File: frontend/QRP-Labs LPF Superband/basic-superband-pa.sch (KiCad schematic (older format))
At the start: 67 parts, among them CN1 EDGE, K1 D3002, K2 D3002, P1 BNC, P2 VFWD, P3 Ext PTT, P4 12-13.8v, Q1 FDV301, Q2 FDV301, Q3 RD16HHF1, T2 8:1, T3 4:1, T4 OUT_TRANSF, U1 LP2951-50D

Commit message: New pre-v2 files
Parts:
- removed C2, C3: 0.1 uF, HERMESLITE:C_0805, symbol Csmall
- removed C26, C4: 0.1uF, HERMESLITE:C_0805, symbol C
- removed CN1: EDGE, HERMESLITE:EDGE, symbol EDGE
- removed D1: YEL LED (Band1), LEDs:LED-0805, symbol LED
- removed D2: RED LED (PTT), LEDs:LED-0805, symbol LED
- removed D3: GRN LED (PWR ON), LEDs:LED-0805, symbol LED
- removed D4: DIODESCH2, HERMESLITE:SOD323, symbol DIODESCH2
- removed FB1: FB, Resistors_SMD:R_0805_HandSoldering, symbol FB
- removed K1, K2: D3002, HERMESLITE:D3002, symbol D3002
- removed P? (x4): CONN_01X04, symbol CONN_01X04
- removed Q1, Q2: FDV301, HERMESLITE:SOT-23-GDS, symbol MOSFET_N
- removed R1, R2: 499, Resistors_SMD:R_0805_HandSoldering, symbol R
- removed R13, R14, R3, R9: 4.99k, Resistors_SMD:R_0805_HandSoldering, symbol R
- removed R15, R16: 10k, Resistors_SMD:R_0805_HandSoldering, symbol R
- removed R4: 0, Resistors_SMD:R_0805_HandSoldering, symbol R
- removed T2: 8:1, HERMESLITE:TRANSF, symbol TRANSF
- removed T3: 4:1, HERMESLITE:TRANSF, symbol TRANSF
- added K1: HK4100, symbol HK4100
- added P1: PA Control, symbol CONN_01X10
- added P2: RX IN, symbol CONN_01X02
- P3: value Ext PTT -> TX-IN; footprint Pin_Headers:Pin_Header_Straight_1x02 -> (none)
- P4: renamed from P1; value BNC -> Antenna
- renumbered C18 to C1, C12 to C10, C16 to C11, C17 to C12, C28 to C13, C29 to C14, C1 to C15, C19 to C16, C20 to C17, C21 to C18, C22 to C19, C23 to C2, C24 to C3, C25 to C4, C27 to C5, C30 to C6, C31 to C7, C7 to C8, C15 to C9, L5 to L1, L6 to L2, L7 to L3, L10 to L4, P2 to P5, P4 to P6, Q3 to Q1, R10 to R1, R11 to R2, R12 to R3, R5 to R4, R6 to R5, R7 to R6, R8 to R7, T4 to T1
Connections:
- net /PTT: now also K1.2, P1.8 (P8)
- net GND: now also P1.10 (P10), P2.1 (P1)
- net at C5.1, L3.2: now also K1.1
- net at T1.4 (SA): now also C14.1; no longer C14.2
- net at P3.2 (P2): now also R1.2, R2.2
- net at C1.2: now also K1.3
- net at C2.1, L1.1: now also P2.2 (P2)
- new net +5V: K1.5, P1.9 (P9)
- new net Band0: P1.1 (P1)
- new net Band1: P1.2 (P2)
- new net Band2: P1.3 (P3)
- new net Band3: P1.4 (P4)
- new net Band4: P1.5 (P5)
- new net Band5: P1.6 (P6)
- new net Band6: P1.7 (P7)
- new net TX-IN: K1.6
- new net TX-OUT: C14.2
- now unconnected: P5.2 (P2)
- no-connect marks 16 -> 3
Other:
- note removed: "(Omit K2 and wire directly \nif only 1 band pair desired)"
- note removed: "4T bifilar\n6T\nBN-61-2402"
- note removed: "6T bifilar\n4T\nBN-61-2402"
- note removed: "Can Omit LEDs if desired"
- note removed: "Ext PTT - active high, 12V"
- note removed: "PTT - RX=low, TX=high\nUSEROUT4 = Band Select 0 = low,\nBand Select 1 = high"
- moved on the sheet: C1, C14, C2, C3, C4, C5, C6, C7, C8, L1, L2, L3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

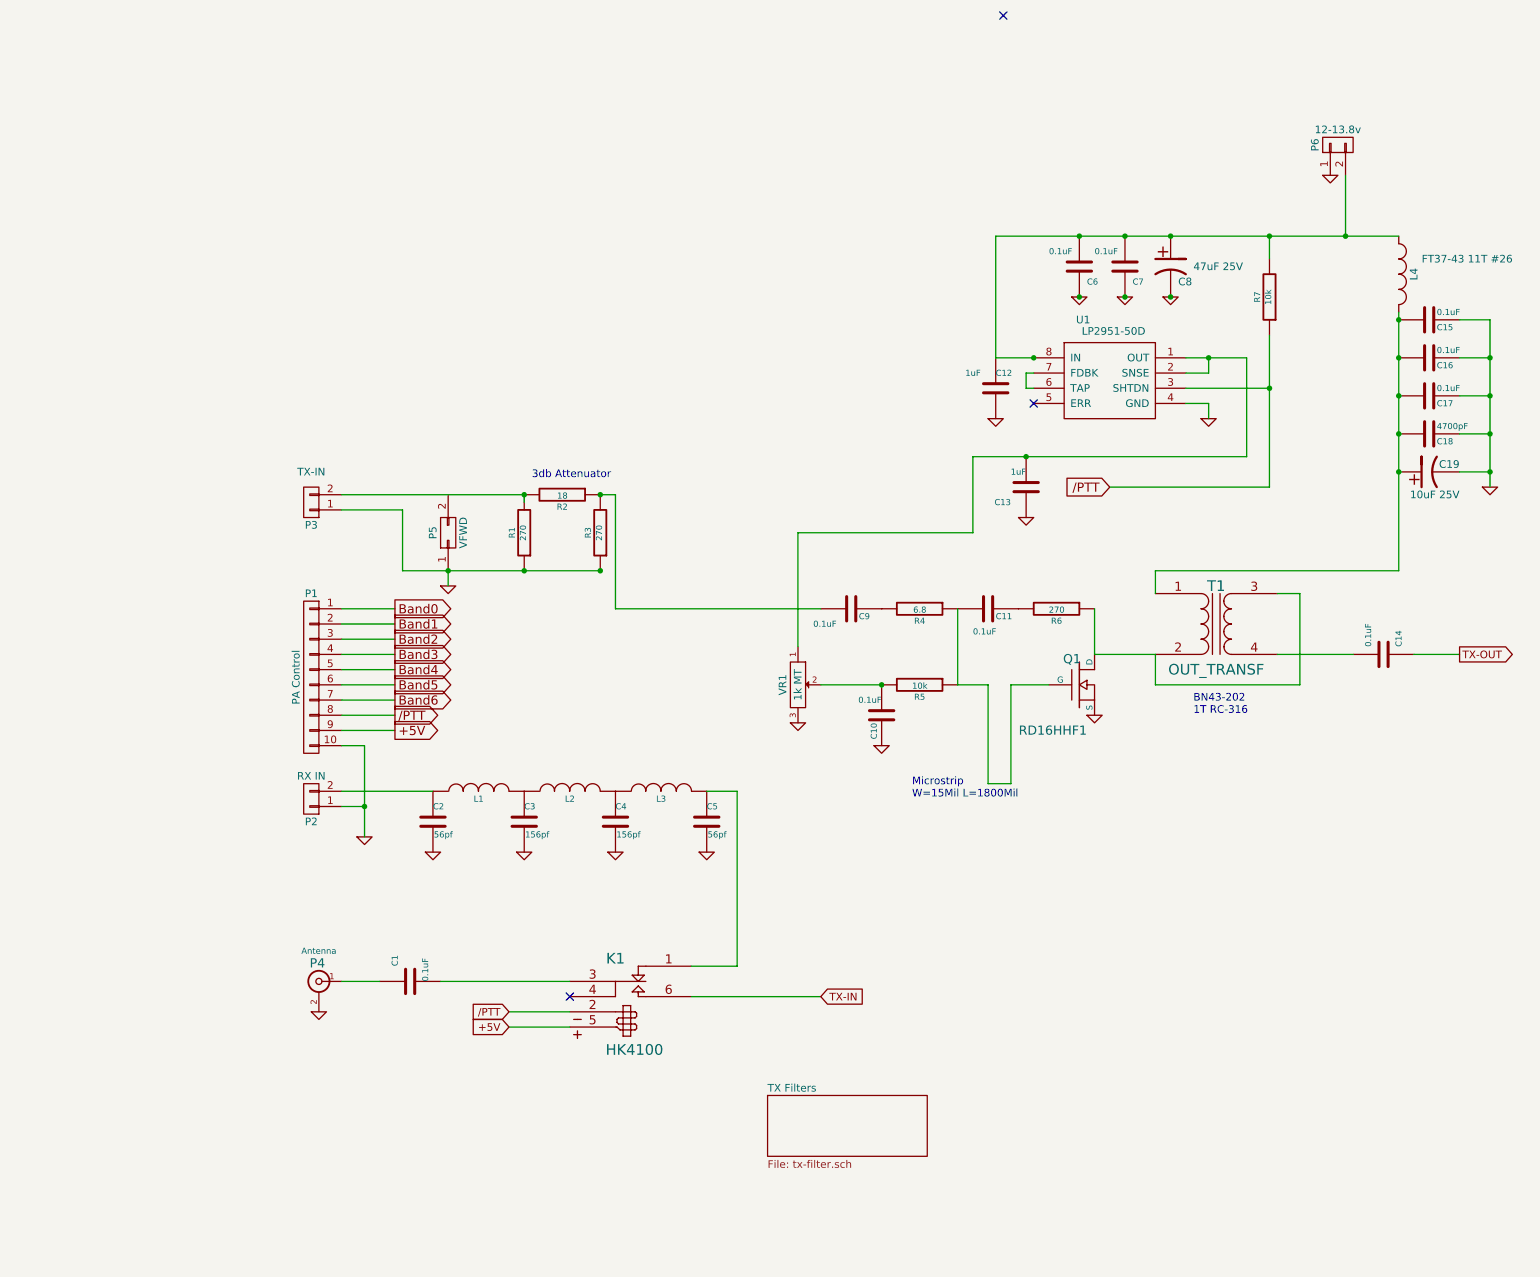
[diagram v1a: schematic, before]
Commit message: Further updates to the pre-V2 amp
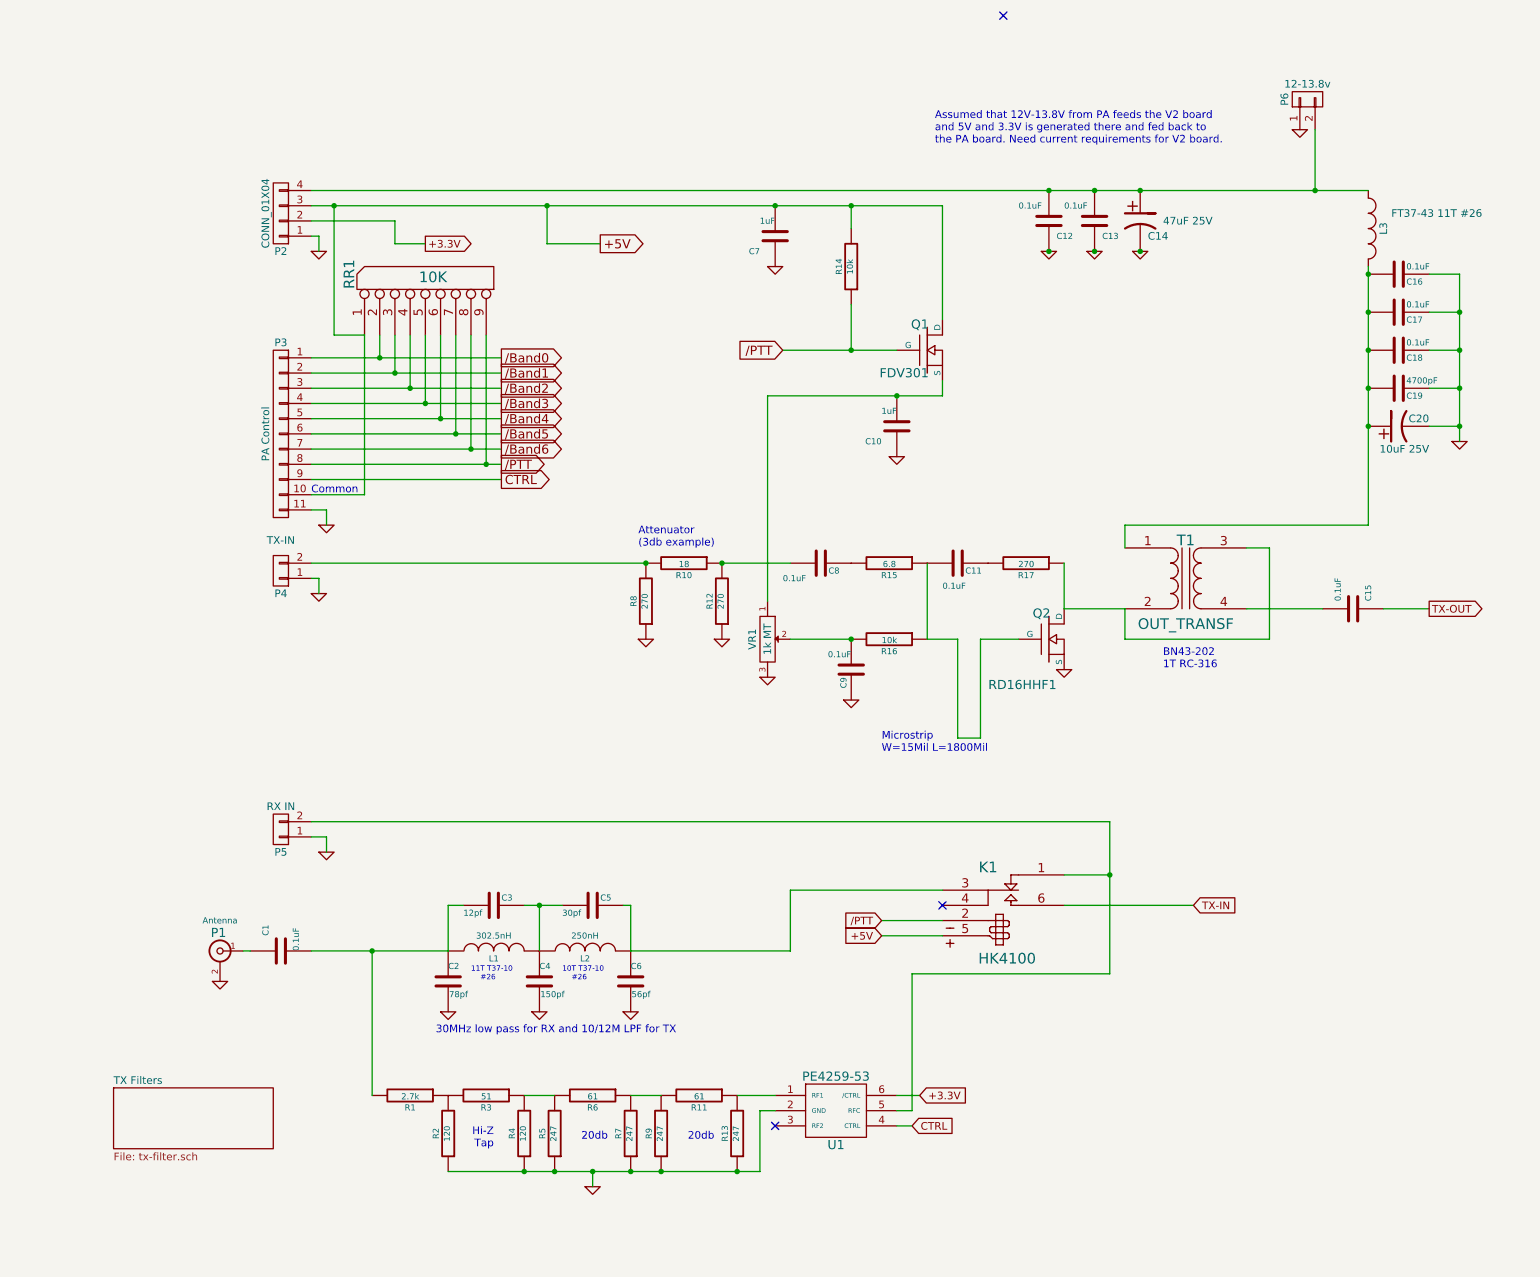
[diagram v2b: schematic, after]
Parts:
- removed C12: 1uF, HERMESLITE:C_0805, symbol C
- removed L3: INDUCTOR, Choke_SMD:Choke_SMD_1206_Standard, symbol INDUCTOR
- removed P1: PA Control, symbol CONN_01X10
- removed P5: VFWD, Pin_Headers:Pin_Header_Straight_1x02, symbol CONN_02X01
- removed U1: LP2951-50D, Housings_SOIC:SOIC-8_3.9x4.9mm_Pitch1.27mm, symbol LP2951-50D
- added C3: 12pf, HERMESLITE:C_0805, symbol C
- added C7: 1uF, HERMESLITE:C_0805, symbol C
- added P2: CONN_01X04, Pin_Headers:Pin_Header_Straight_1x04, symbol CONN_01X04
- added P3: PA Control, Pin_Headers:Pin_Header_Straight_1x11, symbol CONN_01X11
- added Q1: FDV301, HERMESLITE:SOT-23-GDS, symbol MOSFET_N
- added R1: 2.7k, Resistors_SMD:R_0805_HandSoldering, symbol R
- added R11, R6: 61, Resistors_SMD:R_0805_HandSoldering, symbol R
- added R13, R5, R7, R9: 247, Resistors_SMD:R_0805_HandSoldering, symbol R
- added R2, R4: 120, Resistors_SMD:R_0805_HandSoldering, symbol R
- added R3: 51, Resistors_SMD:R_0805_HandSoldering, symbol R
- added RR1: 10K, Discret:r_pack8, symbol RR8
- added U1: PE4259-53, HERMESLITE:sc70-6, symbol PE4259-53
- C2: value 56pf -> 78pf
- C4: renamed from C3; value 156pf -> 150pf
- C5: value 56pf -> 30pf
- C6: renamed from C4; value 156pf -> 56pf
- K1: footprint (none) -> HERMESLITE:HK4100
- L1: value INDUCTOR -> 302.5nH; footprint Choke_SMD:Choke_SMD_1206_Standard -> Choke_Toroid_ThroughHole:Choke_Toroid_5x10mm_Vertical
- L2: value INDUCTOR -> 250nH; footprint Choke_SMD:Choke_SMD_1206_Standard -> Choke_Toroid_ThroughHole:Choke_Toroid_5x10mm_Vertical
- P4: renamed from P3; footprint (none) -> Pin_Headers:Pin_Header_Straight_1x02
- P5: renamed from P2; footprint (none) -> Pin_Headers:Pin_Header_Straight_1x02
- renumbered C13 to C10, C6 to C12, C7 to C13, C8 to C14, C14 to C15, C15 to C16, C16 to C17, C17 to C18, C18 to C19, C19 to C20, C9 to C8, C10 to C9, L4 to L3, P4 to P1, Q1 to Q2, R2 to R10, R3 to R12, R7 to R14, R4 to R15, R5 to R16, R6 to R17, R1 to R8
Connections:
- net +5V: now also R14.2, C7.2, P2.3 (P3), P3.10 (P10), Q1.3 (D), RR1.1 (COM)
- net /PTT: now also P3.8 (P8), Q1.1 (G), RR1.9
- net GND: now also C7.1, P2.1 (P1), P3.11 (P11), R13.1, R2.1, R4.1, R5.1, R7.1, R9.1, U1.2 (GND); no longer C5.2
- net at C12.1, C13.1, C14.1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: now also P2.4 (P4); no longer R14.2
- net at C10.2, VR1.1: now also Q1.2 (S)
- net at C2.1, L1.1: now also C1.2, C3.2, R1.2; no longer P5.2 (P2)
- net at C4.1, L1.2, L2.1: now also C5.2, C3.1
- net at C6.1, L2.2: now also C5.1, K1.3
- net at K1.1: now also P5.2 (P2), U1.5 (RFC); no longer C5.1
- new net: R1.1, R2.2, R3.2
- new net: R3.1, R4.2, R5.2, R6.2
- new net: R11.2, R6.1, R7.2, R9.2
- new net: R11.1, R13.2, U1.1 (RF1)
- new net +3.3V: P2.2 (P2), U1.6 (/CTRL)
- new net /Band0: P3.1 (P1), RR1.2
- new net /Band1: P3.2 (P2), RR1.3
- new net /Band2: P3.3 (P3), RR1.4
- new net /Band3: P3.4 (P4), RR1.5
- new net /Band4: P3.5 (P5), RR1.6
- new net /Band5: P3.6 (P6), RR1.7
- new net /Band6: P3.7 (P7), RR1.8
- new net CTRL: P3.9 (P9), U1.4 (CTRL)
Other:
- note added: "10T T37-10\n #26"
- note added: "11T T37-10\n #26"
- note added: "20db"
- note added: "30MHz low pass for RX and 10/12M LPF for TX"
- note added: "Assumed that 12V-13.8V from PA feeds the V2 board\nand 5V and 3.3V is generated there and fed back to\nthe PA board. Need current requirements for V2 board."
- note added: "Attenuator\n(3db example)"
- note added: "Common"
- note added: "Hi-Z\nTap"
- note removed: "3db Attenuator"
- moved on the sheet: C1, C10, C11, C12, C13, C14, C15, C16, C17, C18, C19, C2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
